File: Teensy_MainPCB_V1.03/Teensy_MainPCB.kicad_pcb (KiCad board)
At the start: 2 copper layers, 141.9 x 100 mm, 68 parts, among them J1 ODO_Left ODO_Left, J10 Sonar_R Sonar_R, J11 Cutter Motor Cutter, J12 Sonar_L Sonar_L, J13 P_Right P_Right, J14 Buzzer Buzzer, J15 Button Button, J16 Power_PCB1 Power_PCB1, J17 Power_PCB2 Power_PCB2, J18 Free01_02 Free01_02, J19 P_Left P_Left, J2 I2C2_0 I2C2_0, J20 Can3 Can3, J21 Ser5 Ser5, J22 FreeA16_A17 FreeA16_A17, J23 ESP RFID1 ESP RFID1, J24 ESP RFID2 ESP RFID2, J25 5V IN, J26 ESP I2C ESP32 I2C, J27 ESP Sens1 ESP32 Sens1, J28 ESP FREE ESP32 FREE, J29 3.3V IN, J3 I2C0_0 I2C0_0, J30 I2C1_0 I2C1_0, J31 Ser3 Ser3, J32 ESP Sens2 ESP32 Sens2, J33 ESP I2C/SER ESP32 I2C/SER, J34 On/Off Teensy On/Off, J4 I2C1_1 I2C1_1, J5 Bumper Bumper, J6 ODO_Right ODO_Right, J7 Motor_Right1 Motor_Right1, J8 Motor_Left1 Motor_Left1, J9 Rain Rain, U2 GY-521, U3 Teensy4.1, U4 ESP32-DEVKIT-V1

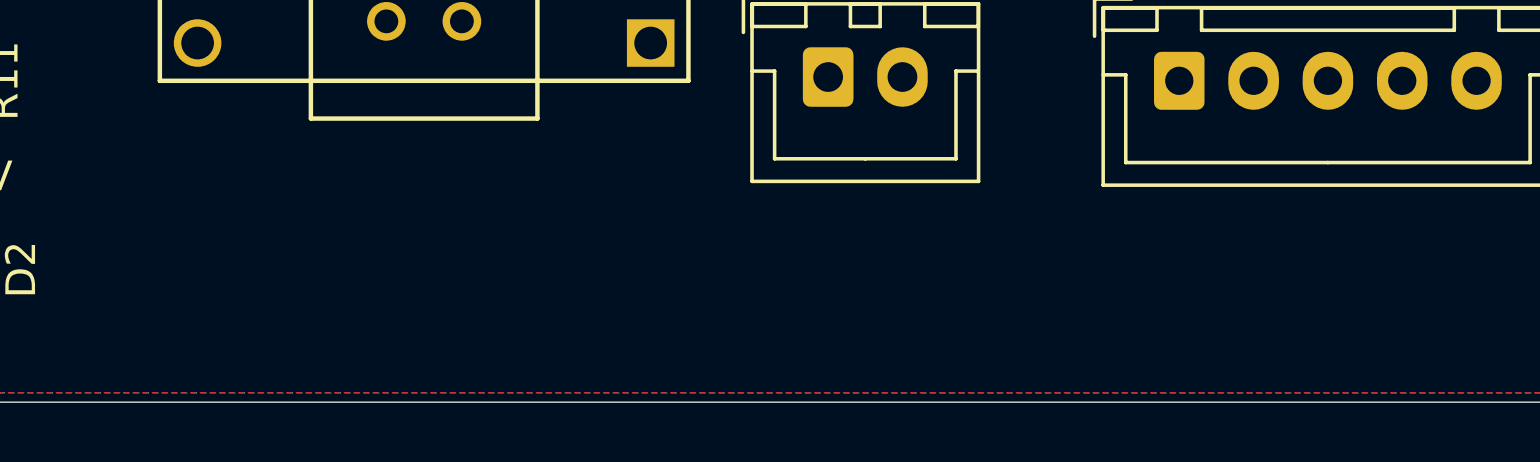
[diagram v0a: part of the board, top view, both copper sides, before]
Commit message: Add Bigger Font
New Version, with bigger Font. At present still without conductors
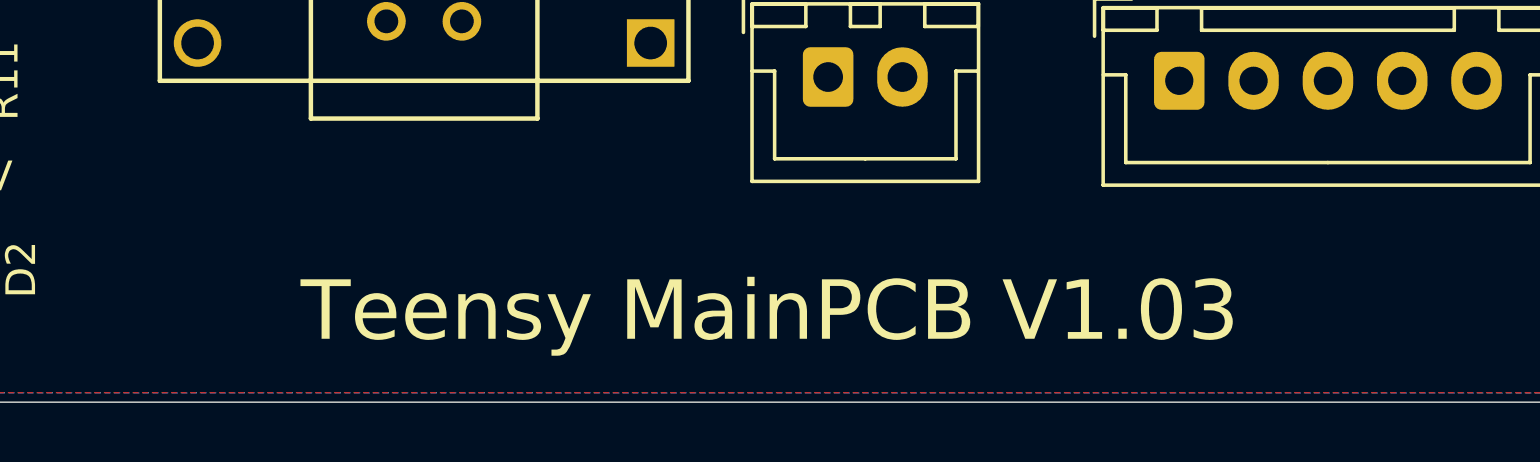
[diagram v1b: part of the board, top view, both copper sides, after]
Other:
- board text added: "Teensy MainPCB V1.03"
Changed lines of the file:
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@@
   (general
     (thickness 1.6)
-    (drawings 95)
+    (drawings 96)
     (tracks 0)
     (zones 0)
@@
     )
   )
+  (gr_text "Teensy MainPCB V1.03" (at 84.0232 130.94208) (layer F.SilkS)
+    (effects (font (size 2 2) (thickness 0.25)))
+  )
   (gr_text IN (at 99.97948 62.57036 -90) (layer F.SilkS)

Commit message: Add Schematic PDF
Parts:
- J1: renamed from J1 ODO_Left; value ODO_Left -> ODO_Right
- J10: renamed from J10 Sonar_R
- J11: renamed from J11 Cutter Motor
- J12: renamed from J12 Sonar_L
- J13: renamed from J13 P_Right
- J14: renamed from J14 Buzzer
- J15: renamed from J15 Button
- J16: renamed from J16 Power_PCB1
- J17: renamed from J17 Power_PCB2
- J18: renamed from J18 Free01_02
- J19: renamed from J19 P_Left
- J2: renamed from J2 I2C2_0
- J20: renamed from J20 Can3
- J21: renamed from J21 Ser5
- J22: renamed from J22 FreeA16_A17
- J23: renamed from J23 ESP RFID1
- J24: renamed from J24 ESP RFID2
- J26: renamed from J26 ESP I2C
- J27: renamed from J27 ESP Sens1
- J28: renamed from J28 ESP FREE
- J3: renamed from J3 I2C0_0
- J30: renamed from J30 I2C1_0
- J31: renamed from J31 Ser3
- J32: renamed from J32 ESP Sens2
- J33: renamed from J33 ESP I2C/SER
- J34: renamed from J34 On/Off
- J4: renamed from J4 I2C1_1
- J5: renamed from J5 Bumper
- J6: renamed from J6 ODO_Right; value ODO_Right -> ODO_Left
- J7: renamed from J7 Motor_Right1
- J8: renamed from J8 Motor_Left1
- J9: renamed from J9 Rain
- JP1: renamed from JP1 Jumper_3.3V
- JP3: renamed from JP3 MotorPower
- JP5: renamed from JP5 CutterPower
- R10, R8: value 1.5KO -> 2KO
- R12, R13: value 1,5KO -> 2KO
- moved R12 13.9 mm to (120.3, 81.8)
- moved R6 13.9 mm to (126.7, 81.8)
- moved R13 13.9 mm to (126.7, 85.6)
- moved R5 13.9 mm to (120.3, 85.6)
- moved J14 10.5 mm to (131.7, 70.1)
- moved J18 10.2 mm to (124.6, 71.2)
- moved J22 4.43 mm to (150.9, 87.5)
- moved J11 3.77 mm to (170.5, 67.5)
- moved J9 2.55 mm to (133.9, 58.3)
- moved J6 2.34 mm to (119.7, 93.9)
- moved J1 2.34 mm to (134.3, 93.9)
- moved J5 2.34 mm to (120.3, 58.2)
- moved J34 1.66 mm to (168.6, 121.2)
- moved U2 1.40 mm to (55.9, 92.6)
- moved SP1 1.06 mm to (169.4, 46.3)
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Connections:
- J24 pad 5: (no net) -> Net-(J24-Pad5)
- R10 pad 1: Net-(J19-Pad3) -> pinPerimeterLeft
- R12 pad 1: Net-(J1-Pad1) -> GND
- R12 pad 2: GND -> pinOdometryRight
- R13 pad 1: Net-(J6-Pad1) -> GND
- R13 pad 2: GND -> pinOdometryLeft
- R7 pad 2: pinPerimeterRight -> Net-(R7-Pad2)
- R8 pad 1: Net-(J13-Pad3) -> Net-(R7-Pad2)
- U2 pad 5: (no net) -> Net-(U2-Pad5)
- U2 pad 6: (no net) -> Net-(U2-Pad6)
- U2 pad 7: (no net) -> Net-(U2-Pad7)
- U2 pad 8: (no net) -> Net-(U2-Pad8)
- U3 pad 1: (no net) -> Net-(U3-Pad1)
- U3 pad 15: (no net) -> Net-(U3-Pad15)
- U3 pad 34: (no net) -> Net-(U3-Pad34)
- U3 pad 49: (no net) -> Net-(U3-Pad49)
- U3 pad 51: (no net) -> Net-(U3-Pad51)
- U3 pad 53: (no net) -> Net-(U3-Pad53)
- U3 pad 55: (no net) -> Net-(U3-Pad55)
- U3 pad 56: (no net) -> Net-(U3-Pad56)
- U3 pad 57: (no net) -> Net-(U3-Pad57)
- U3 pad 58: (no net) -> Net-(U3-Pad58)
- U3 pad 59: (no net) -> Net-(U3-Pad59)
- U3 pad 60: (no net) -> Net-(U3-Pad60)
- U3 pad 61: (no net) -> Net-(U3-Pad61)
- U3 pad 62: (no net) -> Net-(U3-Pad62)
- U3 pad 63: (no net) -> Net-(U3-Pad63)
- U3 pad 64: (no net) -> Net-(U3-Pad64)
- U3 pad 65: (no net) -> Net-(U3-Pad65)
- U3 pad 66: (no net) -> Net-(U3-Pad66)
- U3 pad 67: (no net) -> Net-(U3-Pad67)
- U4 pad 1: (no net) -> Net-(U4-Pad1)
- U4 pad 10: (no net) -> Net-(U4-Pad10)
- U4 pad 17: (no net) -> Net-(U4-Pad17)
- U4 pad 19: (no net) -> Net-(U4-Pad19)
- U4 pad 2: (no net) -> Net-(U4-Pad2)
- U4 pad 23: (no net) -> Net-(U4-Pad23)
- U4 pad 3: (no net) -> Net-(U4-Pad3)
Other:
- board text added: "Buzzer"
- board text removed: "PinBuzzer"

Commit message: Front Correction
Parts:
- moved J22 9.34 mm to (156.5, 94.9), turned to 180 degrees
- moved JP3 2.58 mm to (161.8, 58.3)
- moved JP5 1.67 mm to (171.8, 58.4)
- moved J34 1.62 mm to (170.2, 121.2)
- moved R14 0.95 mm to (140.1, 118.4)
- moved R15 0.95 mm to (146.3, 118.4)
- moved J31 0.95 mm to (174.8, 98.8)
- moved J8 0.88 mm to (159.4, 67.1)
- moved R17 0.86 mm to (173.6, 107.7)
- moved R16 0.84 mm to (167.1, 107.7)
- moved R19 0.80 mm to (173.6, 114.0)
- moved R18 0.79 mm to (167.1, 114.0)
- moved J11 0.71 mm to (169.9, 67.2)
- moved J7 0.71 mm to (147.5, 67.0)
- moved J21 0.61 mm to (174.8, 86.9)
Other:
- board text added: "CRX3"
- board text added: "CTX3"
- board text removed: "+5V"

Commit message: First Route
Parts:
- moved R12 9.21 mm to (129.5, 82.1)
- moved R5 9.21 mm to (129.5, 85.9)
- moved R13 8.29 mm to (118.4, 86.0)
- moved R6 8.29 mm to (118.4, 82.2)
- moved J15 6.05 mm to (90.2, 127.4)
- moved J20 5.01 mm to (100.8, 127.2)
- moved U3 1.95 mm to (70.6, 93.4)
- moved BT1 1.23 mm to (134.3, 47.4)
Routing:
- net GND: track 0.00 -> 649.0 mm
- net +3V3: track 0.00 -> 399.1 mm
- net +5V: track 0.00 -> 366.8 mm, vias 0 -> 2
- net Net-(J34-Pad1): track 0.00 -> 162.5 mm
- net RX3: track 0.00 -> 158.7 mm
- net Net-(J34-Pad2): track 0.00 -> 153.9 mm
- net pinMotorMowDir: track 0.00 -> 125.9 mm
- net pinBuzzer: track 0.00 -> 123.9 mm
- net SDA1: track 0.00 -> 123.7 mm
- net TX5: track 0.00 -> 121.6 mm
- net TX3: track 0.00 -> 120.4 mm, vias 0 -> 1
- net pinMotorMowEnable: track 0.00 -> 119.2 mm, vias 0 -> 1
- net pinMotorMowPWM: track 0.00 -> 118.5 mm
- net RX5: track 0.00 -> 117.4 mm
- net Net-(JP1-Pad3): track 0.00 -> 117.0 mm
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- removed copper zone on B.Cu, net GND
- removed copper zone on F.Cu, net GND

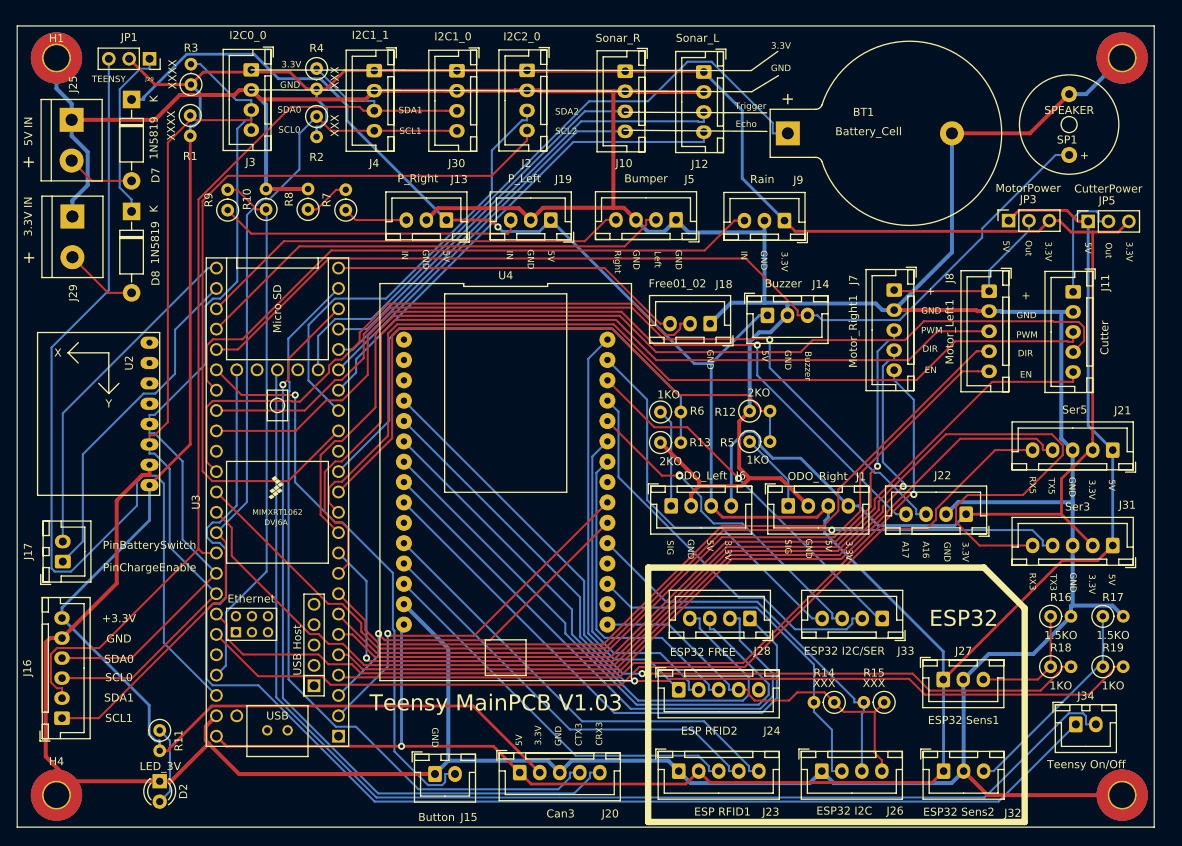
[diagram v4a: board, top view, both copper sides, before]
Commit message: Add GND Plane
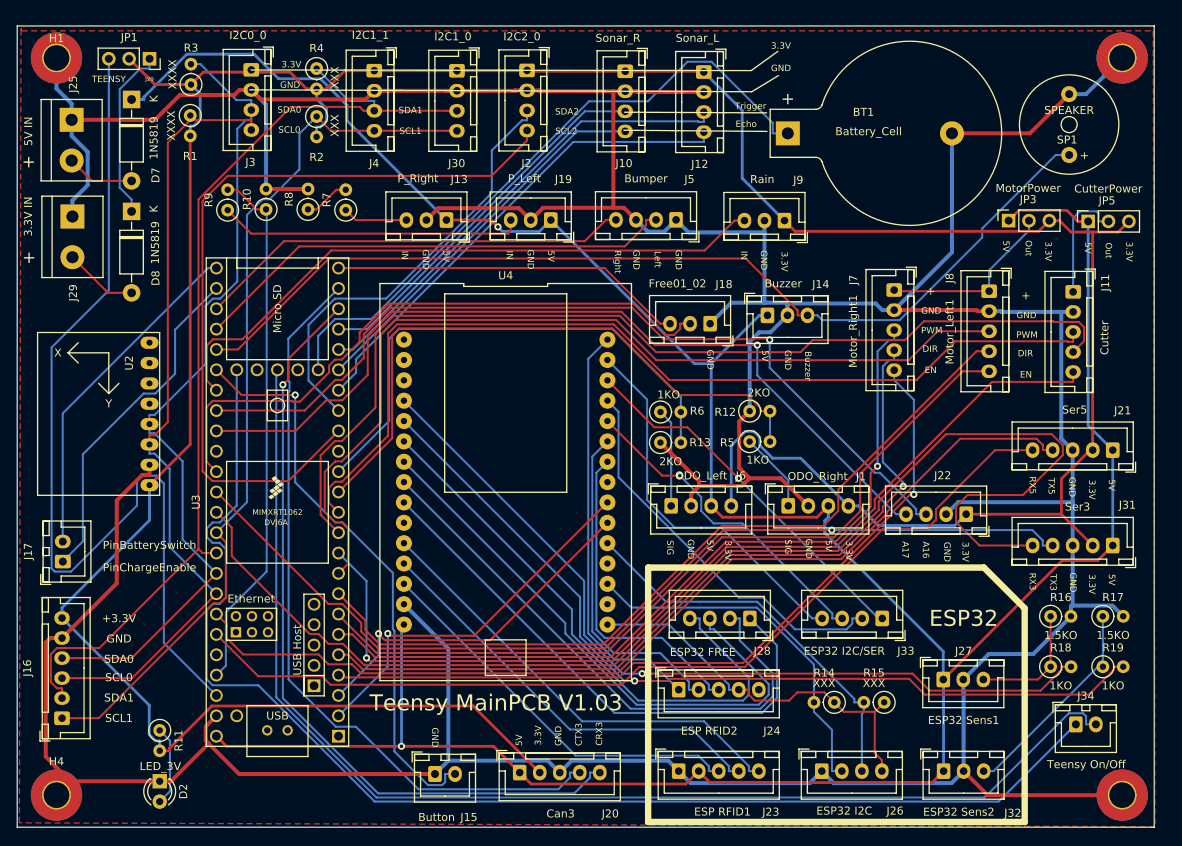
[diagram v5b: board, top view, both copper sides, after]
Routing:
- added copper zone on F.Cu, net GND
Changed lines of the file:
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@@
     (46 B.CrtYd user)
     (47 F.CrtYd user)
-    (48 B.Fab user hide)
+    (48 B.Fab user)
     (49 F.Fab user)
   )
@@
   (segment (start 77.9197 54.448) (end 75.4697 56.898) (width 0.254) (layer F.Cu) (net 82))
   (segment (start 75.4697 56.898) (end 74.391 56.898) (width 0.254) (layer F.Cu) (net 82))
+  (zone (net 3) (net_name GND) (layer F.Cu) (hatch edge 0.508)
+    (connect_pads (clearance 0.508))
+    (min_thickness 0.254)
+    (fill yes (arc_segments 32) (thermal_gap 0.508) (thermal_bridge_width 0.508))
+    (polygon
+      (pts
+        (xy 38.5953 34.3535) (xy 38.569802 34.3535) (xy 38.569784 34.362657) (xy 38.63594 34.61258) (xy 179.87518 34.61258)
+        (xy 180.09362 133.94436) (xy 38.36924 133.45922) (xy 38.569784 34.362657) (xy 38.56736 34.3535) (xy 38.569802 34.3535)
+        (xy 38.5699 34.30524)
+      )
+    )
+  )
 )

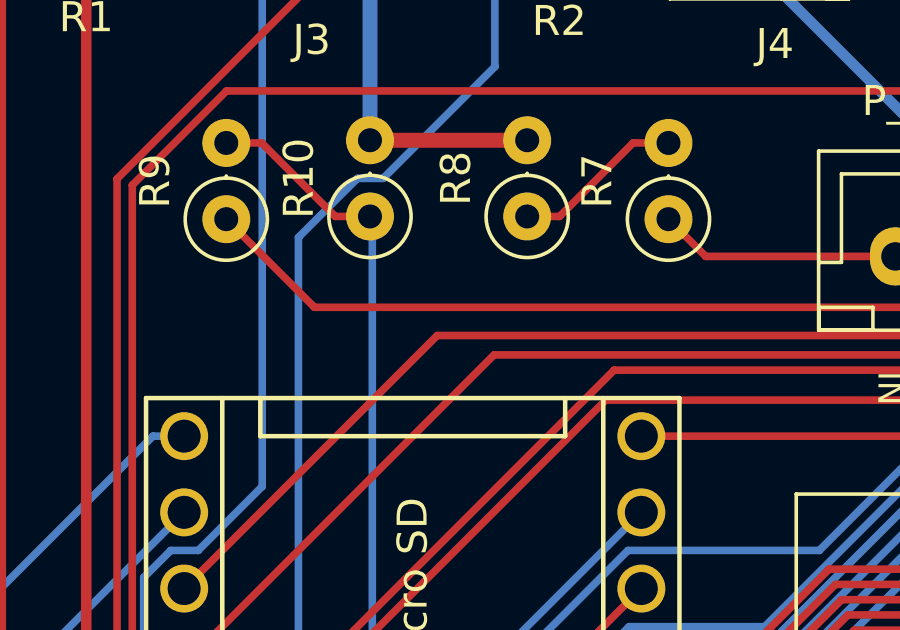
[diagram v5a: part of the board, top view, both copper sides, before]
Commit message: Small Changes in Labelling
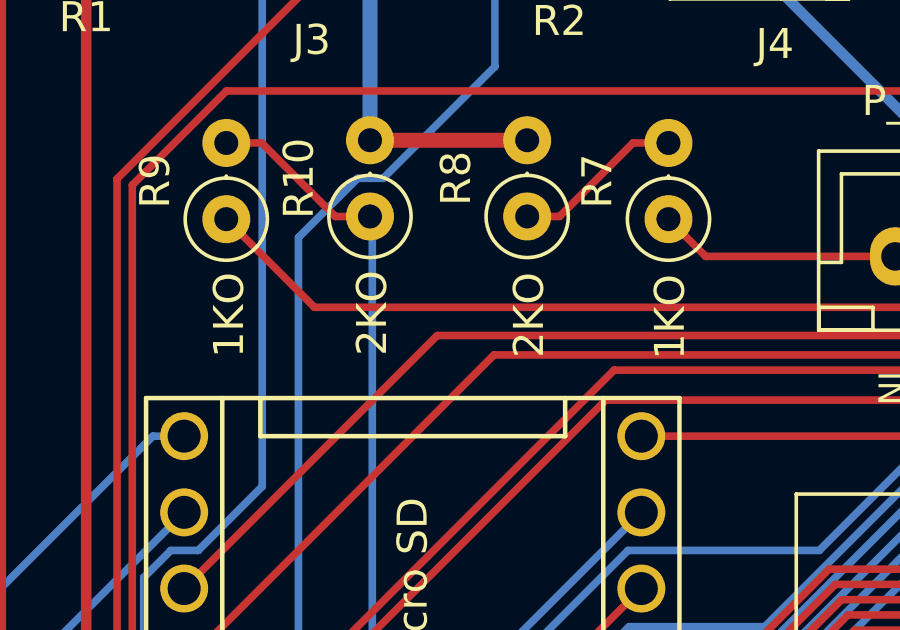
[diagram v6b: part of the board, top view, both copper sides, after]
